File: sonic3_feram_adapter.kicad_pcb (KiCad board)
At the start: 2 copper layers, 17.8 x 30.5 mm, 2 parts, among them IC1 FM16W08-SG, P1 CONN_02X12

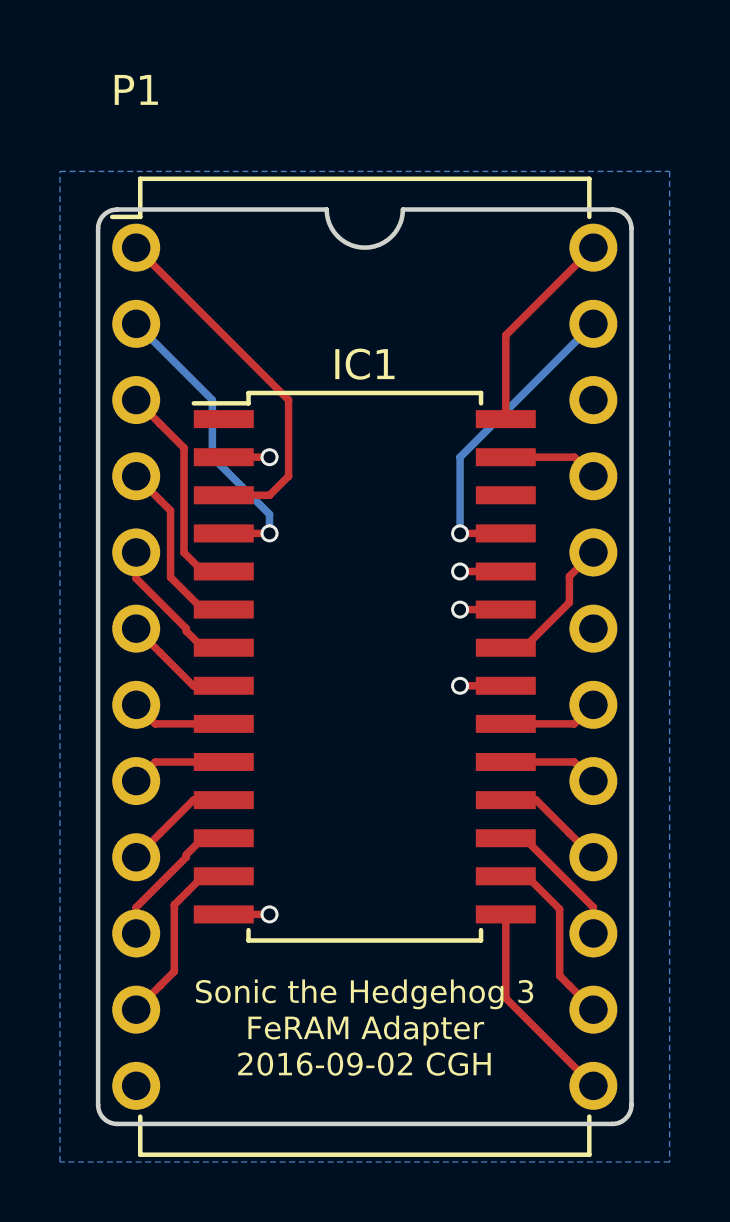
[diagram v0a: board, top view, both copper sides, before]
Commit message: Added jumpers for bank selection
Since this board adapts an 8 KiB chip to work in the place of a 512 B
chip, it seems like it would be nice to allow the user to change which
block of 512 B is in use.  To allow this, I added solder bump jumpers to
the high address lines so they can be pulled to ground or 5 V.
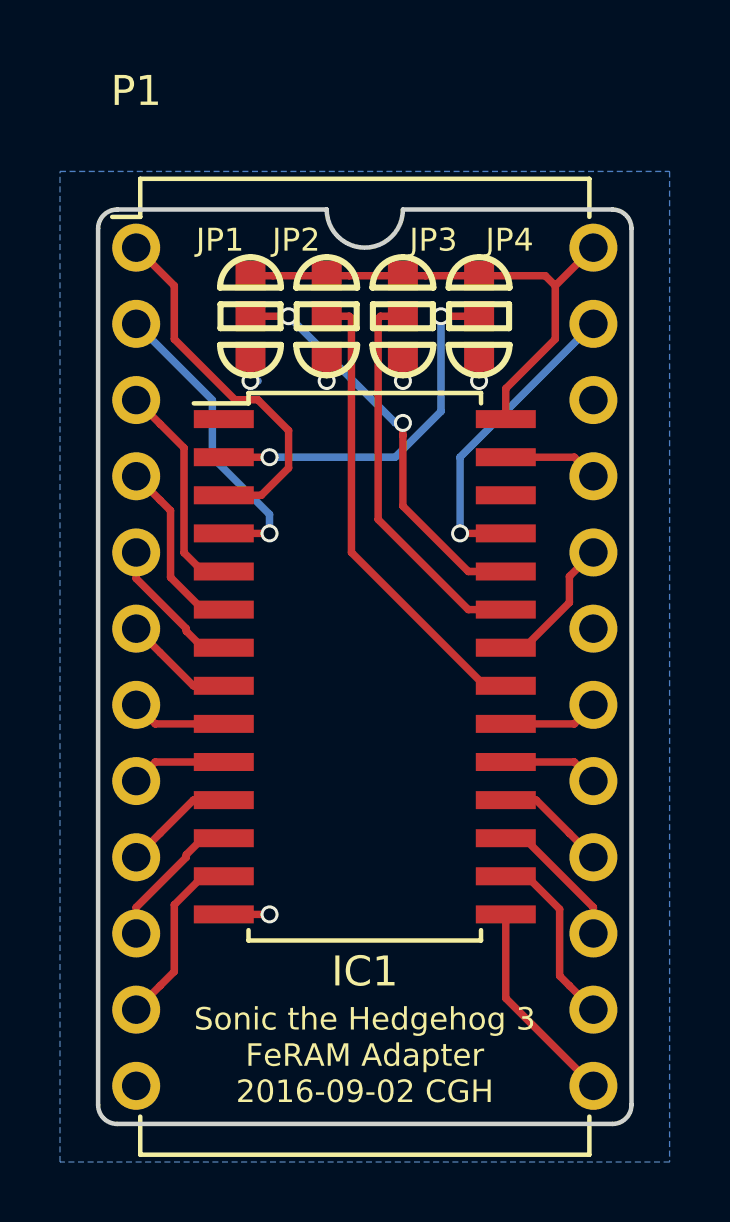
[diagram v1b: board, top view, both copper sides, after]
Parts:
- added JP1: JUMPER3, jumper:SOLDER-JUMPER_2-WAY, F.Cu at (72.4, 64.5)
- added JP2: JUMPER3, jumper:SOLDER-JUMPER_2-WAY, F.Cu at (74.9, 64.5)
- added JP3: JUMPER3, jumper:SOLDER-JUMPER_2-WAY, F.Cu at (77.5, 64.5)
- added JP4: JUMPER3, jumper:SOLDER-JUMPER_2-WAY, F.Cu at (80.0, 64.5)
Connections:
- IC1 pad 2: GND -> Net-(IC1-Pad2)
- IC1 pad 21: GND -> Net-(IC1-Pad21)
- IC1 pad 23: GND -> Net-(IC1-Pad23)
- IC1 pad 24: GND -> Net-(IC1-Pad24)
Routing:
- net Net-(IC1-Pad21): track 0.00 -> 15.6 mm
- net Net-(IC1-Pad24): track 0.00 -> 13.7 mm, vias 0 -> 2
- net Net-(IC1-Pad23): track 0.00 -> 13.1 mm
- net Net-(IC1-Pad2): track 0.00 -> 12.3 mm, vias 0 -> 2
- net +5V: track 6.92 -> 17.2 mm
- net GND: track 7.63 -> 5.02 mm
